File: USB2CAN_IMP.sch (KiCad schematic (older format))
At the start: 24 parts

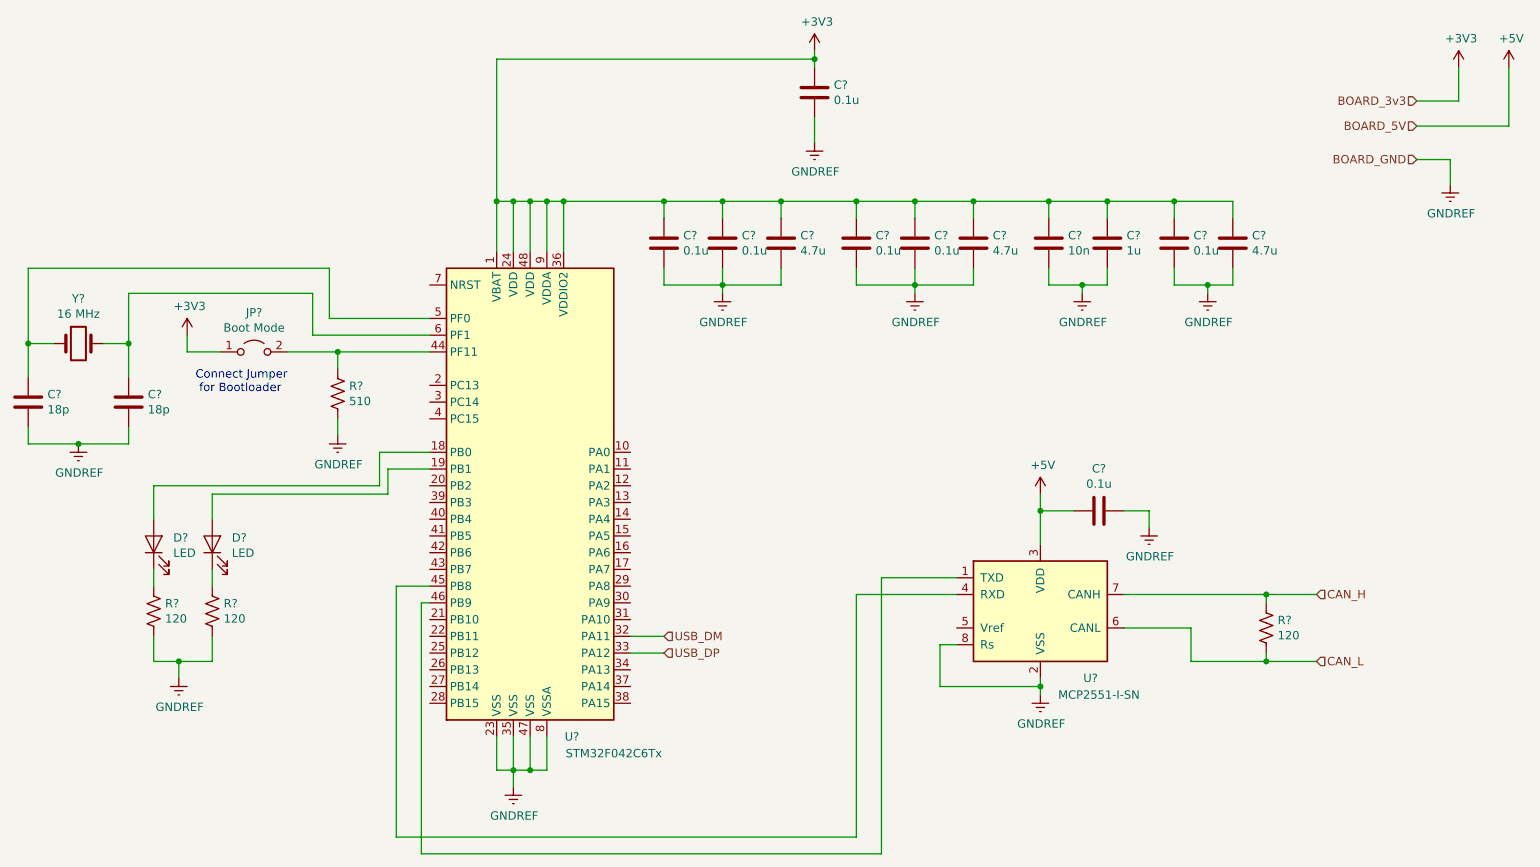
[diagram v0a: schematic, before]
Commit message: Added labels to all components
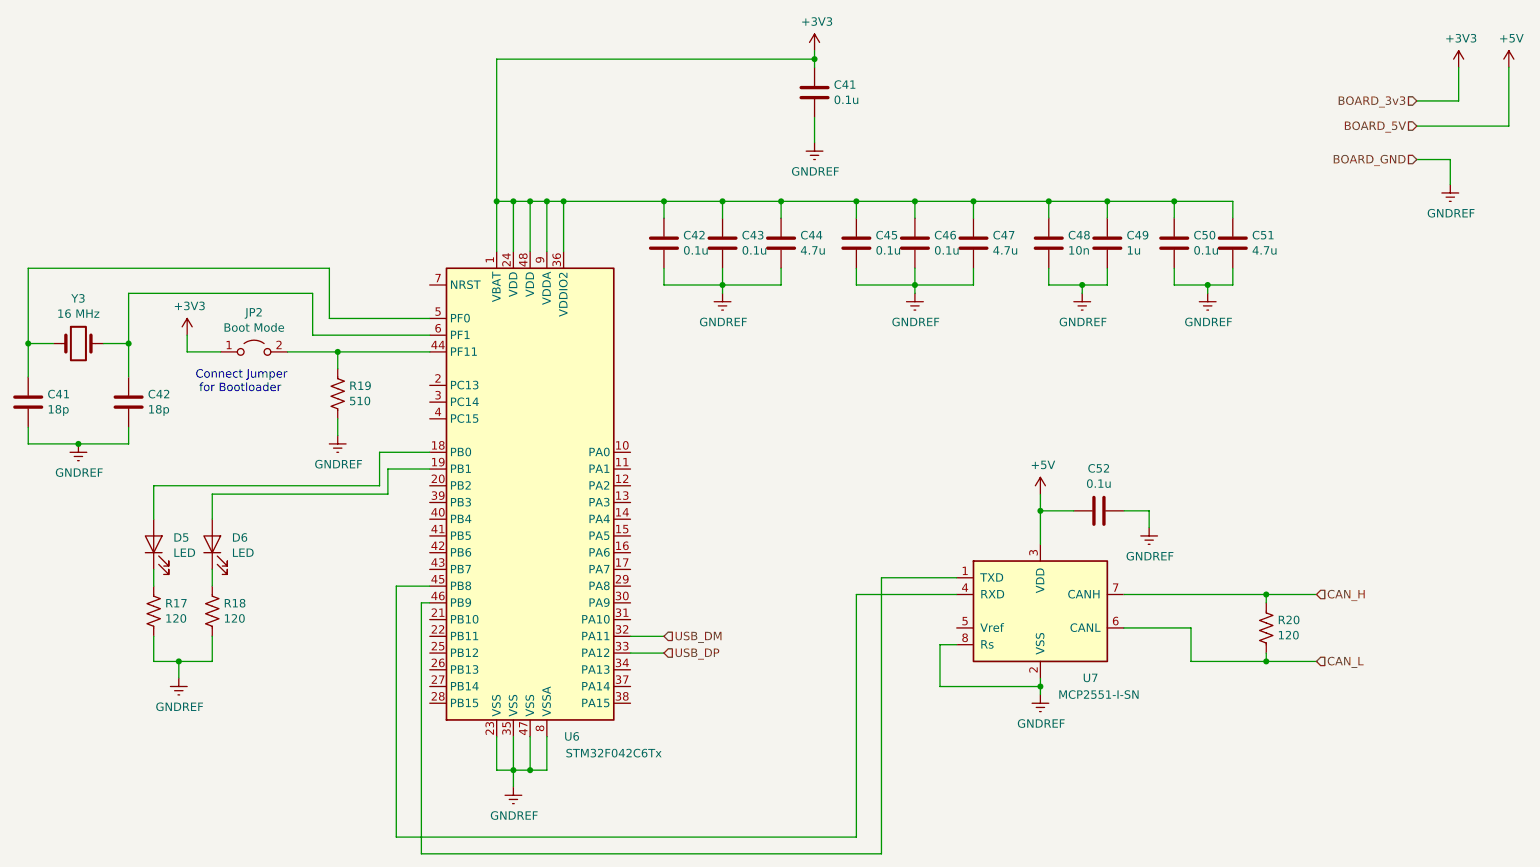
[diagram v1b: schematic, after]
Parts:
- gave numbers to parts that had none: 22
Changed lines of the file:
@@
 P 4350 3400
 AR Path="/5E564EEA/5E5656C2" Ref="U?"  Part="1"
-AR Path="/5E45C906/5E5656C2" Ref="U?"  Part="1"
-F 0 "U?" H 4600 1900 50  0000 C CNN
+AR Path="/5E45C906/5E5656C2" Ref="U6"  Part="1"
+F 0 "U6" H 4600 1900 50  0000 C CNN
 F 1 "STM32F042C6Tx" H 4850 1800 50  0000 C CNN
 F 2 "Package_QFP:LQFP-48_7x7mm_P0.5mm" H 3850 2000 50  0001 R CNN
@@
 P 6050 1050
 AR Path="/5E564EEA/5E56F9CC" Ref="C?"  Part="1"
-AR Path="/5E45C906/5E56F9CC" Ref="C?"  Part="1"
-F 0 "C?" H 6165 1096 50  0000 L CNN
+AR Path="/5E45C906/5E56F9CC" Ref="C41"  Part="1"
+F 0 "C41" H 6165 1096 50  0000 L CNN
 F 1 "0.1u" H 6165 1005 50  0000 L CNN
 F 2 "" H 6088 900 50  0001 C CNN
@@
 P 5150 1950
 AR Path="/5E564EEA/5E570D68" Ref="C?"  Part="1"
-AR Path="/5E45C906/5E570D68" Ref="C?"  Part="1"
-F 0 "C?" H 5265 1996 50  0000 L CNN
+AR Path="/5E45C906/5E570D68" Ref="C42"  Part="1"
+F 0 "C42" H 5265 1996 50  0000 L CNN
 F 1 "0.1u" H 5265 1905 50  0000 L CNN
 F 2 "" H 5188 1800 50  0001 C CNN
@@
 P 5500 1950
 AR Path="/5E564EEA/5E571AEF" Ref="C?"  Part="1"
-AR Path="/5E45C906/5E571AEF" Ref="C?"  Part="1"
-F 0 "C?" H 5615 1996 50  0000 L CNN
+AR Path="/5E45C906/5E571AEF" Ref="C43"  Part="1"
+F 0 "C43" H 5615 1996 50  0000 L CNN
 F 1 "0.1u" H 5615 1905 50  0000 L CNN
 F 2 "" H 5538 1800 50  0001 C CNN
@@
 P 5850 1950
 AR Path="/5E564EEA/5E571D74" Ref="C?"  Part="1"
-AR Path="/5E45C906/5E571D74" Ref="C?"  Part="1"
-F 0 "C?" H 5965 1996 50  0000 L CNN
+AR Path="/5E45C906/5E571D74" Ref="C44"  Part="1"
+F 0 "C44" H 5965 1996 50  0000 L CNN
 F 1 "4.7u" H 5965 1905 50  0000 L CNN
 F 2 "" H 5888 1800 50  0001 C CNN
@@
 P 6300 1950
 AR Path="/5E564EEA/5E57AEE1" Ref="C?"  Part="1"
-AR Path="/5E45C906/5E57AEE1" Ref="C?"  Part="1"
-F 0 "C?" H 6415 1996 50  0000 L CNN
+AR Path="/5E45C906/5E57AEE1" Ref="C45"  Part="1"
+F 0 "C45" H 6415 1996 50  0000 L CNN
 F 1 "0.1u" H 6415 1905 50  0000 L CNN
 F 2 "" H 6338 1800 50  0001 C CNN
@@
 P 6650 1950
 AR Path="/5E564EEA/5E57B1AF" Ref="C?"  Part="1"
-AR Path="/5E45C906/5E57B1AF" Ref="C?"  Part="1"
-F 0 "C?" H 6765 1996 50  0000 L CNN
+AR Path="/5E45C906/5E57B1AF" Ref="C46"  Part="1"
+F 0 "C46" H 6765 1996 50  0000 L CNN
 F 1 "0.1u" H 6765 1905 50  0000 L CNN
 F 2 "" H 6688 1800 50  0001 C CNN
@@
 P 7000 1950
 AR Path="/5E564EEA/5E57B49C" Ref="C?"  Part="1"
-AR Path="/5E45C906/5E57B49C" Ref="C?"  Part="1"
-F 0 "C?" H 7115 1996 50  0000 L CNN
+AR Path="/5E45C906/5E57B49C" Ref="C47"  Part="1"
+F 0 "C47" H 7115 1996 50  0000 L CNN
 F 1 "4.7u" H 7115 1905 50  0000 L CNN
 F 2 "" H 7038 1800 50  0001 C CNN
@@
 P 7450 1950
 AR Path="/5E564EEA/5E584EC0" Ref="C?"  Part="1"
-AR Path="/5E45C906/5E584EC0" Ref="C?"  Part="1"
-F 0 "C?" H 7565 1996 50  0000 L CNN
+AR Path="/5E45C906/5E584EC0" Ref="C48"  Part="1"
+F 0 "C48" H 7565 1996 50  0000 L CNN
 F 1 "10n" H 7565 1905 50  0000 L CNN
 F 2 "" H 7488 1800 50  0001 C CNN
@@
 P 7800 1950
 AR Path="/5E564EEA/5E5855D5" Ref="C?"  Part="1"
-AR Path="/5E45C906/5E5855D5" Ref="C?"  Part="1"
-F 0 "C?" H 7915 1996 50  0000 L CNN
+AR Path="/5E45C906/5E5855D5" Ref="C49"  Part="1"
+F 0 "C49" H 7915 1996 50  0000 L CNN
 F 1 "1u" H 7915 1905 50  0000 L CNN
 F 2 "" H 7838 1800 50  0001 C CNN
@@
 P 8200 1950
 AR Path="/5E564EEA/5E5893FA" Ref="C?"  Part="1"
-AR Path="/5E45C906/5E5893FA" Ref="C?"  Part="1"
-F 0 "C?" H 8315 1996 50  0000 L CNN
+AR Path="/5E45C906/5E5893FA" Ref="C50"  Part="1"
+F 0 "C50" H 8315 1996 50  0000 L CNN
 F 1 "0.1u" H 8315 1905 50  0000 L CNN
 F 2 "" H 8238 1800 50  0001 C CNN
@@
 P 8550 1950
 AR Path="/5E564EEA/5E5897D1" Ref="C?"  Part="1"
-AR Path="/5E45C906/5E5897D1" Ref="C?"  Part="1"
-F 0 "C?" H 8665 1996 50  0000 L CNN
+AR Path="/5E45C906/5E5897D1" Ref="C51"  Part="1"
+F 0 "C51" H 8665 1996 50  0000 L CNN
 F 1 "4.7u" H 8665 1905 50  0000 L CNN
 F 2 "" H 8588 1800 50  0001 C CNN
@@
 P 7400 4150
 AR Path="/5E564EEA/5E59148C" Ref="U?"  Part="1"
-AR Path="/5E45C906/5E59148C" Ref="U?"  Part="1"
-F 0 "U?" H 7700 3750 50  0000 C CNN
+AR Path="/5E45C906/5E59148C" Ref="U7"  Part="1"
+F 0 "U7" H 7700 3750 50  0000 C CNN
 F 1 "MCP2551-I-SN" H 7750 3650 50  0000 C CNN
 F 2 "Package_SO:SOIC-8_3.9x4.9mm_P1.27mm" H 7400 3650 50  0001 C CIN
@@
 P 7750 3550
 AR Path="/5E564EEA/5E596828" Ref="C?"  Part="1"
-AR Path="/5E45C906/5E596828" Ref="C?"  Part="1"
-F 0 "C?" V 7498 3550 50  0000 C CNN
+AR Path="/5E45C906/5E596828" Ref="C52"  Part="1"
+F 0 "C52" V 7498 3550 50  0000 C CNN
 F 1 "0.1u" V 7589 3550 50  0000 C CNN
 F 2 "" H 7788 3400 50  0001 C CNN
@@
 P 2700 2600
 AR Path="/5E564EEA/5E5AAE77" Ref="JP?"  Part="1"
-AR Path="/5E45C906/5E5AAE77" Ref="JP?"  Part="1"
-F 0 "JP?" H 2700 2835 50  0000 C CNN
+AR Path="/5E45C906/5E5AAE77" Ref="JP2"  Part="1"
+F 0 "JP2" H 2700 2835 50  0000 C CNN
 F 1 "Boot Mode" H 2700 2744 50  0000 C CNN
 F 2 "" H 2700 2600 50  0001 C CNN
@@
 P 3200 2850
 AR Path="/5E564EEA/5E5B42BD" Ref="R?"  Part="1"
-AR Path="/5E45C906/5E5B42BD" Ref="R?"  Part="1"
-F 0 "R?" H 3268 2896 50  0000 L CNN
+AR Path="/5E45C906/5E5B42BD" Ref="R19"  Part="1"
+F 0 "R19" H 3268 2896 50  0000 L CNN
 F 1 "510" H 3268 2805 50  0000 L CNN
 F 2 "" V 3240 2840 50  0001 C CNN
@@
 P 1950 2900
 AR Path="/5E564EEA/5E5BF702" Ref="C?"  Part="1"
-AR Path="/5E45C906/5E5BF702" Ref="C?"  Part="1"
-F 0 "C?" H 2065 2946 50  0000 L CNN
+AR Path="/5E45C906/5E5BF702" Ref="C42"  Part="1"
+F 0 "C42" H 2065 2946 50  0000 L CNN
 F 1 "18p" H 2065 2855 50  0000 L CNN
 F 2 "" H 1988 2750 50  0001 C CNN
@@
 P 1650 2550
 AR Path="/5E564EEA/5E5BFCE2" Ref="Y?"  Part="1"
-AR Path="/5E45C906/5E5BFCE2" Ref="Y?"  Part="1"
-F 0 "Y?" H 1650 2818 50  0000 C CNN
+AR Path="/5E45C906/5E5BFCE2" Ref="Y3"  Part="1"
+F 0 "Y3" H 1650 2818 50  0000 C CNN
 F 1 "16 MHz" H 1650 2727 50  0000 C CNN
 F 2 "" H 1650 2550 50  0001 C CNN
@@
 P 1350 2900
 AR Path="/5E564EEA/5E5C064C" Ref="C?"  Part="1"
-AR Path="/5E45C906/5E5C064C" Ref="C?"  Part="1"
-F 0 "C?" H 1465 2946 50  0000 L CNN
+AR Path="/5E45C906/5E5C064C" Ref="C41"  Part="1"
+F 0 "C41" H 1465 2946 50  0000 L CNN
 F 1 "18p" H 1465 2855 50  0000 L CNN
 F 2 "" H 1388 2750 50  0001 C CNN
@@
 P 2100 3750
 AR Path="/5E564EEA/5E5D4B83" Ref="D?"  Part="1"
-AR Path="/5E45C906/5E5D4B83" Ref="D?"  Part="1"
-F 0 "D?" V 2139 3633 50  0000 R CNN
+AR Path="/5E45C906/5E5D4B83" Ref="D5"  Part="1"
+F 0 "D5" V 2139 3633 50  0000 R CNN
 F 1 "LED" V 2048 3633 50  0000 R CNN
 F 2 "" H 2100 3750 50  0001 C CNN
@@
 P 2450 3750
 AR Path="/5E564EEA/5E5D53D6" Ref="D?"  Part="1"
-AR Path="/5E45C906/5E5D53D6" Ref="D?"  Part="1"
-F 0 "D?" V 2489 3633 50  0000 R CNN
+AR Path="/5E45C906/5E5D53D6" Ref="D6"  Part="1"
+F 0 "D6" V 2489 3633 50  0000 R CNN
 F 1 "LED" V 2398 3633 50  0000 R CNN
 F 2 "" H 2450 3750 50  0001 C CNN
@@
 P 2100 4150
 AR Path="/5E564EEA/5E5DDB72" Ref="R?"  Part="1"
-AR Path="/5E45C906/5E5DDB72" Ref="R?"  Part="1"
-F 0 "R?" H 2168 4196 50  0000 L CNN
+AR Path="/5E45C906/5E5DDB72" Ref="R17"  Part="1"
+F 0 "R17" H 2168 4196 50  0000 L CNN
 F 1 "120" H 2168 4105 50  0000 L CNN
 F 2 "" V 2140 4140 50  0001 C CNN
@@
 P 2450 4150
 AR Path="/5E564EEA/5E5DE222" Ref="R?"  Part="1"
-AR Path="/5E45C906/5E5DE222" Ref="R?"  Part="1"
-F 0 "R?" H 2518 4196 50  0000 L CNN
+AR Path="/5E45C906/5E5DE222" Ref="R18"  Part="1"
+F 0 "R18" H 2518 4196 50  0000 L CNN
 F 1 "120" H 2518 4105 50  0000 L CNN
 F 2 "" V 2490 4140 50  0001 C CNN
@@
 P 8750 4250
 AR Path="/5E564EEA/5E5FF6DC" Ref="R?"  Part="1"
-AR Path="/5E45C906/5E5FF6DC" Ref="R?"  Part="1"
-F 0 "R?" H 8818 4296 50  0000 L CNN
+AR Path="/5E45C906/5E5FF6DC" Ref="R20"  Part="1"
+F 0 "R20" H 8818 4296 50  0000 L CNN
 F 1 "120" H 8818 4205 50  0000 L CNN
 F 2 "" V 8790 4240 50  0001 C CNN
